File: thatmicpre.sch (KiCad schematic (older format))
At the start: 79 parts, among them J1 Barrel_Jack_Switch, J2 NC3FBH1, J3 NC3MBH2, Q1 BC546C, Q2 BC546C, SW1 SW_DPDT_x2, SW2 SW_DPDT_x2, SW3 SW_Rotary12, U1 THAT1510P08-U

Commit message: Update to v1.1.
Add gerbers and pdfs to plots.
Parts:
- removed D11, D12, D7, D9: MBR160, Diode_THT:D_DO-34_SOD68_P7.62mm_Horizontal, symbol Device:D_Schottky
- removed R11: 1Meg, Resistor_THT:R_Axial_DIN0207_L6.3mm_D2.5mm_P10.16mm_Horizontal, symbol Device:R_US
- removed R12: 27k, Resistor_THT:R_Axial_DIN0207_L6.3mm_D2.5mm_P10.16mm_Horizontal, symbol Device:R_US
- added D18, D19: 1N4148, Diode_THT:D_DO-34_SOD68_P7.62mm_Horizontal, symbol Device:D
- added D7: 1N4004, Diode_THT:D_DO-41_SOD81_P10.16mm_Horizontal, symbol Device:D
- added F1: Polyfuse, Fuse:Fuse_BelFuse_0ZRE0005FF_L8.3mm_W3.8mm, symbol Device:Polyfuse
- added LOGO2: Logo_Open_Hardware_Small, Symbol:Symbol_CC-Attribution_CopperTop_Small, symbol Graphic:Logo_Open_Hardware_Small
- added LOGO3: Logo_Open_Hardware_Small, Symbol:Symbol_CreativeCommons_CopperTop_Type2_Small, symbol Graphic:Logo_Open_Hardware_Small
- added LOGO4: SYM_Arrow_Normal, Symbol:Symbol_Barrel_Polarity, symbol Graphic:SYM_Arrow_Normal
- added R8: 47k, Resistor_THT:R_Axial_DIN0207_L6.3mm_D2.5mm_P10.16mm_Horizontal, symbol Device:R_US
- C1, C2: Vendor (none) -> RDE5C2A471J0M1H03A
- C10, C12, C7, C8: Vendor (none) -> UPW1J221MPD
- C11: value 220u-63V -> 47u-50V; footprint Capacitor_THT:CP_Radial_D10.0mm_P5.00mm -> Capacitor_THT:CP_Radial_D6.3mm_P2.50mm; Vendor (none) -> UFW1H470MED1TD
- C13: value 2200u-6V3 -> 3300u-6V3; Vendor (none) -> UFW0J332MPD
- C14, C16, C19: value 10u-63V -> 47u-50V; Vendor (none) -> UFW1H470MED1TD
- C15, C17, C9: Vendor (none) -> PHE426DJ5100JR05
- C18: value 220u-63V -> 1000u-25V; Vendor (none) -> UVZ1E102MPD1CM
- C3: Vendor (none) -> RDE5C2A470J0M1H03A
- C4, C5: value 47u-63V -> 47u-63V-BP; Vendor (none) -> UVP1J470MPD
- C6: Vendor (none) -> R82EC3100AA70J
- D1, D2, D3, D4: Vendor (none) -> 1N4004GP-E3/54
- D10, D14: Vendor (none) -> LTL-4232N
- D13, D5, D6, D8: Vendor (none) -> 1N4148
- D15, D16, D17: value 15V -> 18V; footprint Diode_THT:D_DO-41_SOD81_P10.16mm_Horizontal -> Diode_THT:D_DO-34_SOD68_P7.62mm_Horizontal; Vendor (none) -> BZX55B18-TAP
- J1: Vendor (none) -> CON-SOCJ-2155
- J2: Vendor (none) -> NC3FBH1
- J3: value NC3MBH2 -> NC3MBH1; symbol Connector:XLR3_Ground -> Connector:XLR3; Vendor (none) -> NC3MBH
- LOGO1: footprint Symbol:OSHW-Logo2_7.3x6mm_SilkScreen -> Symbol:OSHW-Symbol_6.7x6mm_Copper
- Q1, Q2: Vendor (none) -> BC546CTA
- R1, R2: value 1k2 -> 1k2-0.1%; Vendor (none) -> YR1B1K21CC
- R10: value 39k -> 22k; Vendor (none) -> MBB02070C2202FCT00
- R13, R27, R30, R9: Vendor (none) -> MBB02070C1002FCT00
- R14: value 100k -> 1M0; Vendor (none) -> MBB02070C1004FCT00
- R15: Vendor (none) -> MBB02070C2701FC100
- R16: Vendor (none) -> MBB02070C1001FC100
- R17: Vendor (none) -> MBB02070C5600FC100
- R18: Vendor (none) -> MBB02070C2700FC100
- R19: Vendor (none) -> MBB02070C1500FC100
- R20: Vendor (none) -> MFR50SFTE52-82R
- R21: Vendor (none) -> MFR50SFTE52-47R
- R22: Vendor (none) -> MFR50SFTE52-27R
- R23: Vendor (none) -> MFR50SFTE52-15R
- R24: Vendor (none) -> MFR50SFTE52-8R2
- R25: Vendor (none) -> CPF110R000BHE14
- R26, R29: Vendor (none) -> MFR50SFTE52-100R
- R28: value 10k -> 4k7; Vendor (none) -> MBB02070C4701FCT00
- R3, R4: value 10R -> 10R-1W; Vendor (none) -> CPF110R000FEB14
- R5, R6: value 6k8-0.1%-1W -> 6k8-0.1%-0.5W; footprint Resistor_THT:R_Axial_DIN0411_L9.9mm_D3.6mm_P12.70mm_Horizontal -> Resistor_THT:R_Axial_DIN0207_L6.3mm_D2.5mm_P10.16mm_Horizontal; Vendor (none) -> CMF556K8100BEEK
- R7: Vendor (none) -> MBB02070C2202FCT00
- SW1, SW2: Vendor (none) -> 200MDP1T2B2M6QE
- SW3: Vendor (none) -> SR2612F-0112-38F5B-D8-S
- U1: Vendor (none) -> THAT1510P08-U
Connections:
- net GND: now also C9.2, J1.2, D7.2 (A), R8.2; no longer D14.1 (K), J3.G, SW1.1 (A)
- net at C18.1, D17.1 (K), R29.2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: now also D14.1 (K); no longer R28.2
- net at R5.1, R6.1, SW1.2 (B): no longer R10.1, SW1.5 (B)
- net at C8.1, Q1.1 (C), Q2.1 (C)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: now also D18.1 (K), D19.1 (K), D7.1 (K), F1.2
- net at C10.1, D8.1 (K), Q1.2 (B)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: now also D18.2 (A)
- net at C12.1, D13.1 (K), D15.1 (K)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: now also D19.2 (A)
- net at D14.2 (A): now also R28.2
- net at C9.1, J1.1: now also F1.1
- new net: R10.1, SW1.5 (B)
- new net: R8.1, SW1.1 (A)
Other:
- moved on the sheet: C10, C11, C13, C18, C19, C6, C7, D10, D13, D14, D17, D8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

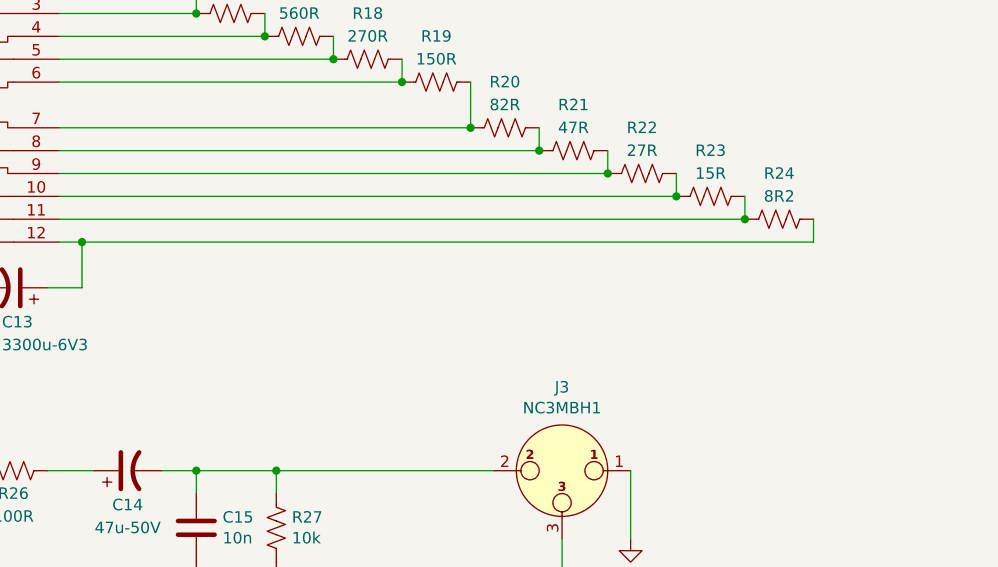
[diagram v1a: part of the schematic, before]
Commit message: Add .m file to calculate gain resistors. Add comment to schematic
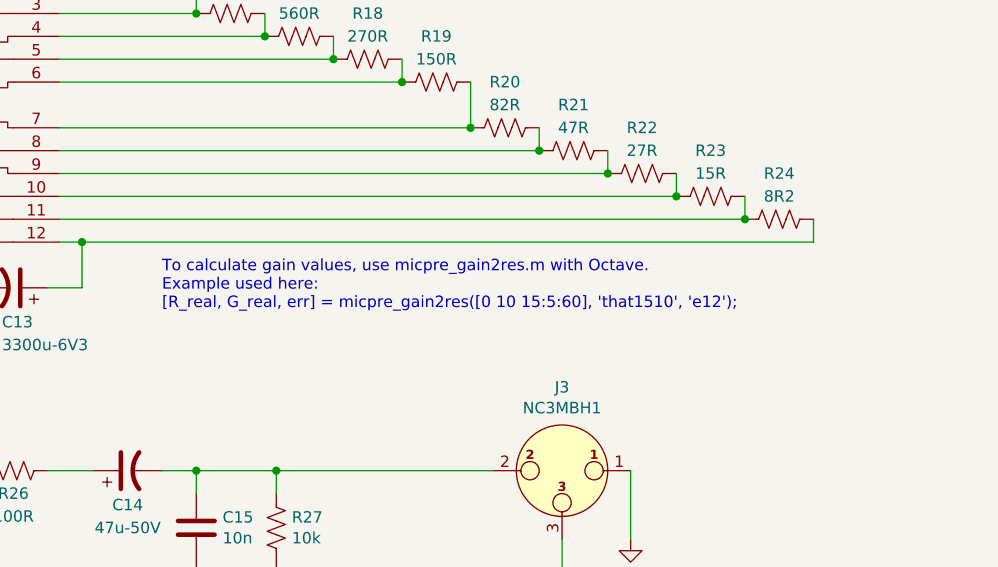
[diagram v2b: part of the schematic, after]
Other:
- note added: "To calculate gain values, use micpre_gain2res.m with Octave.\nExample used here:\n[R_real, G_real, err] = micpre_gain2res([0 10 15:5:60], 'that1510', 'e12');"
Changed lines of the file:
@@
 	-1   0    0    1
 $EndComp
+Text Notes 8100 4200 0    50   ~ 0
+To calculate gain values, use micpre_gain2res.m with Octave.\nExample used here:\n[R_real, G_real, err] = micpre_gain2res([0 10 15:5:60], 'that1510', 'e12');
 $EndSCHEMATC
